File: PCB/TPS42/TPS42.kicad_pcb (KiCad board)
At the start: 2 copper layers, 138.1 x 89.7 mm, 81 parts, among them J1 PJ-320A, J11 Conn_01x06, J13 Conn_01x09, J14 FH12-10S-0.5SH, J2 Conn_01x09, J3 TP Sensor Module, J4 TP Module, J6 OLED, J7 TrackPoint, J8 Battery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

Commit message: Further footprint changes
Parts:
- C1: footprint TPS42:C_THT_SMD_0805_HandSolder_Reversable -> TPS42:C_0603_1608Metric_Pad1.08x0.95mm_HandSolder_Reversable
- C2, C3, C4: footprint Capacitor_SMD:C_0603_1608Metric_Pad1.08x0.95mm_HandSolder -> TPS42:C_0603_1608Metric_Pad1.08x0.95mm_HandSolder_Reversable
- R1, R2, R3, R4, R5: footprint TPS42:Resistor-TH_SMD -> TPS42:R_0603_1608Metric_Pad0.98x0.95mm_HandSolder_Reversable
- R6: footprint Resistor_SMD:R_0603_1608Metric_Pad0.98x0.95mm_HandSolder -> TPS42:R_0603_1608Metric_Pad0.98x0.95mm_HandSolder_Reversable
- moved C1 6.59 mm to (139.9, 172.4)

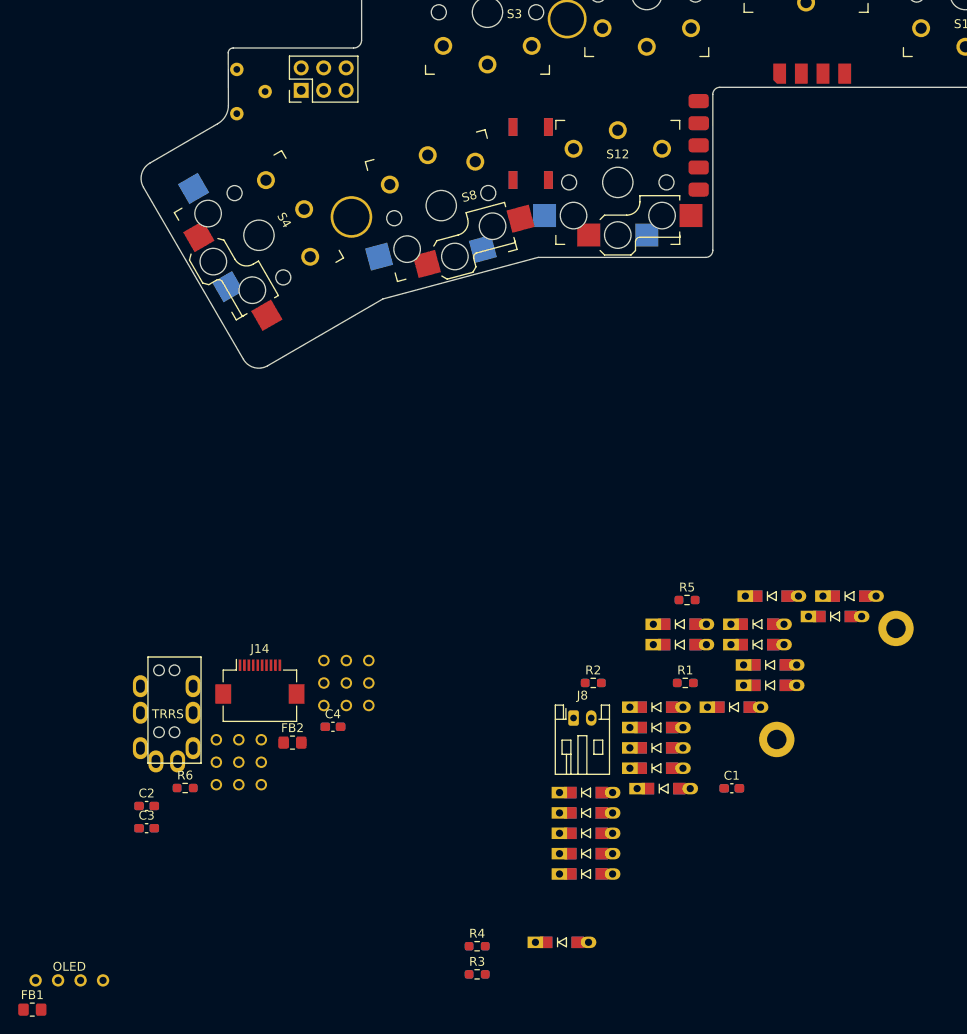
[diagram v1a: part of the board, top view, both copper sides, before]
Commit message: replaced diode footprint
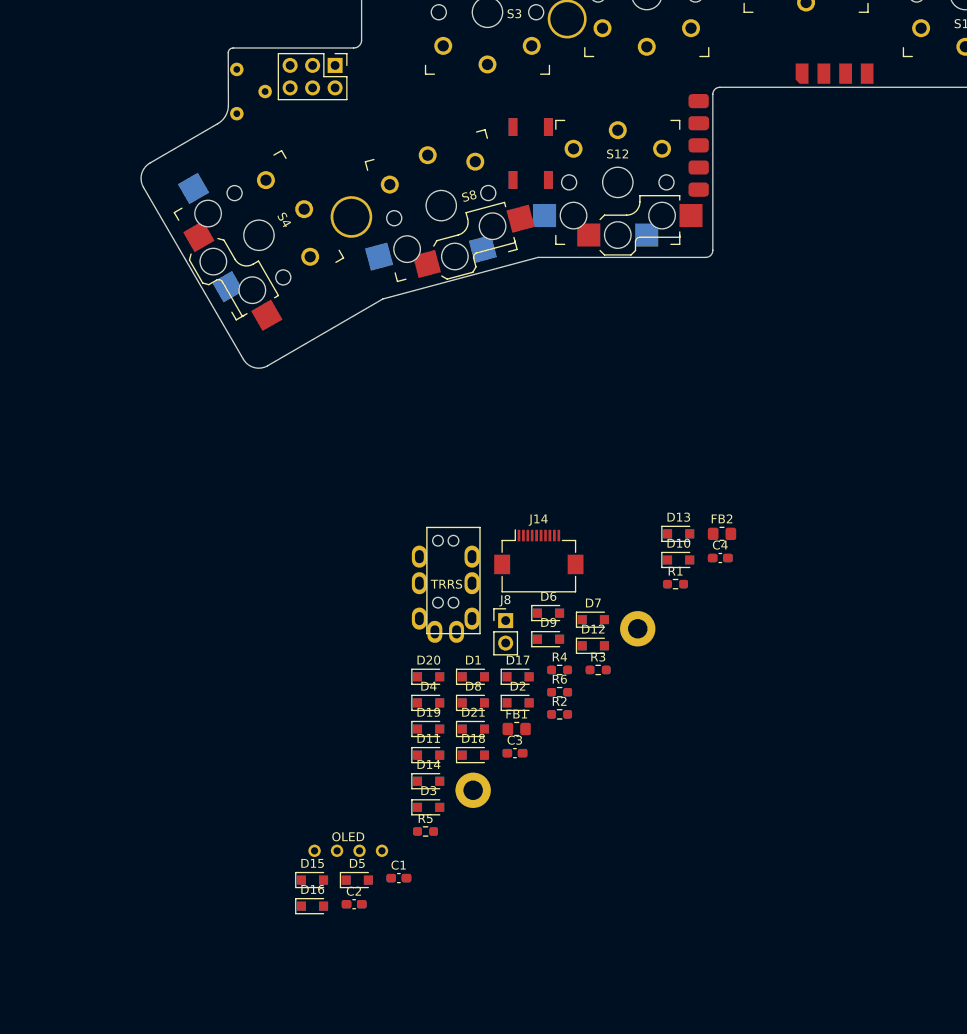
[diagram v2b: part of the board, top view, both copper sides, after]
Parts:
- removed J13, J2: Conn_01x09, TPS42:Connector_Reversable_3x3
- D1, D10, D11, D12, D13, D14, D15, D16, D17, D18, D19, D2, D20, D21, D3, D4, D5, D6, D7, D8, D9: footprint TPS42:D3_TH_SMD_v2 -> TPS42:D_SOD-323_HandSoldering_Reversable
- J8: footprint Connector_JST:JST_PH_S2B-PH-K_1x02_P2.00mm_Horizontal -> Connector_PinHeader_2.54mm:PinHeader_1x02_P2.54mm_Vertical
- moved FB1 63.3 mm to (115.6, 165.7)
- moved D16 59.5 mm to (92.5, 185.8)
- moved FB2 54.0 mm to (138.8, 143.7)
- moved D5 52.5 mm to (97.6, 182.8)
- moved C4 47.7 mm to (138.6, 146.4)
- moved D18 43.8 mm to (110.7, 168.7)
- moved R6 43.7 mm to (120.4, 161.6)
- moved C3 42.5 mm to (115.4, 168.5)
- moved D15 41.6 mm to (92.5, 182.8)
- moved D19 41.6 mm to (105.6, 165.7)
- moved R5 39.5 mm to (105.3, 177.3)
- moved D2 39.3 mm to (115.7, 162.8)
- moved C1 39.0 mm to (102.3, 182.6)
- moved R3 37.0 mm to (124.8, 159.1)
- moved U2 34.8 mm to (110.7, 172.7)
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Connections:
- J11 pad 4: VCC -> SERIAL
- J11 pad 5: SERIAL -> VCC

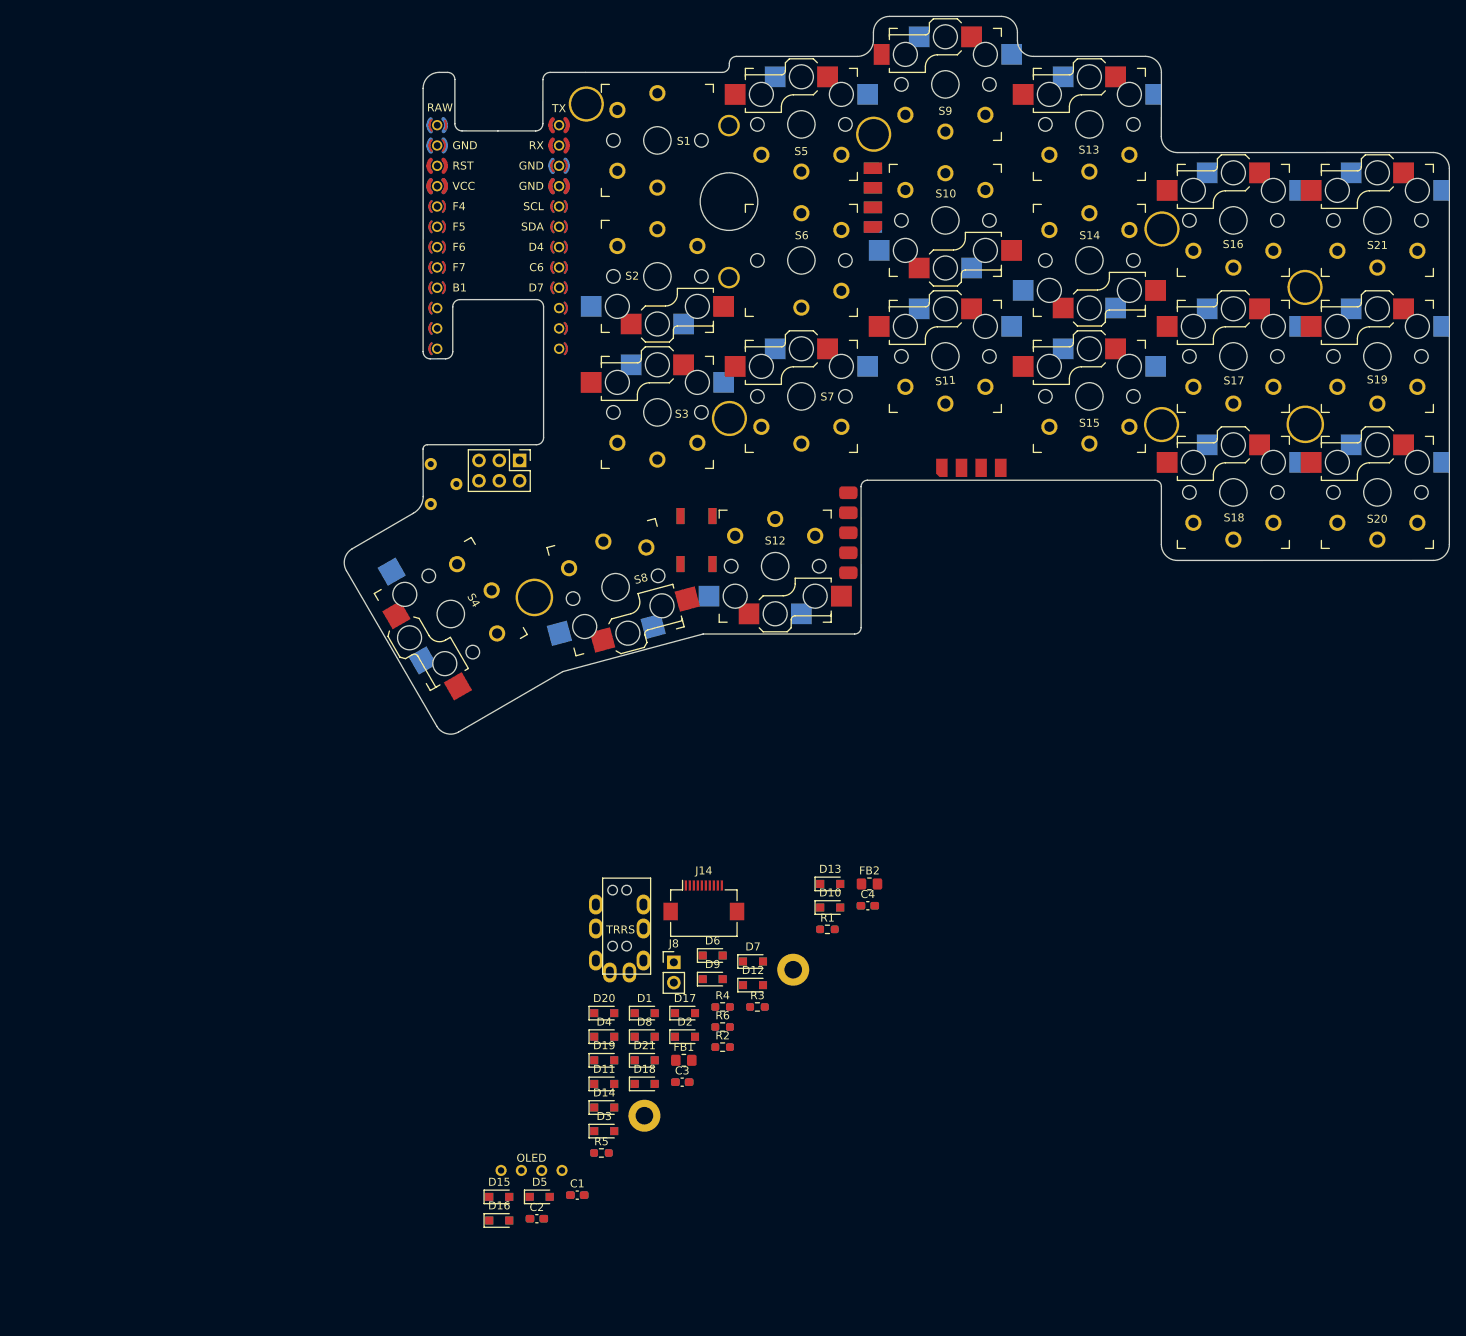
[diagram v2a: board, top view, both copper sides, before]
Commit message: breakoff column added
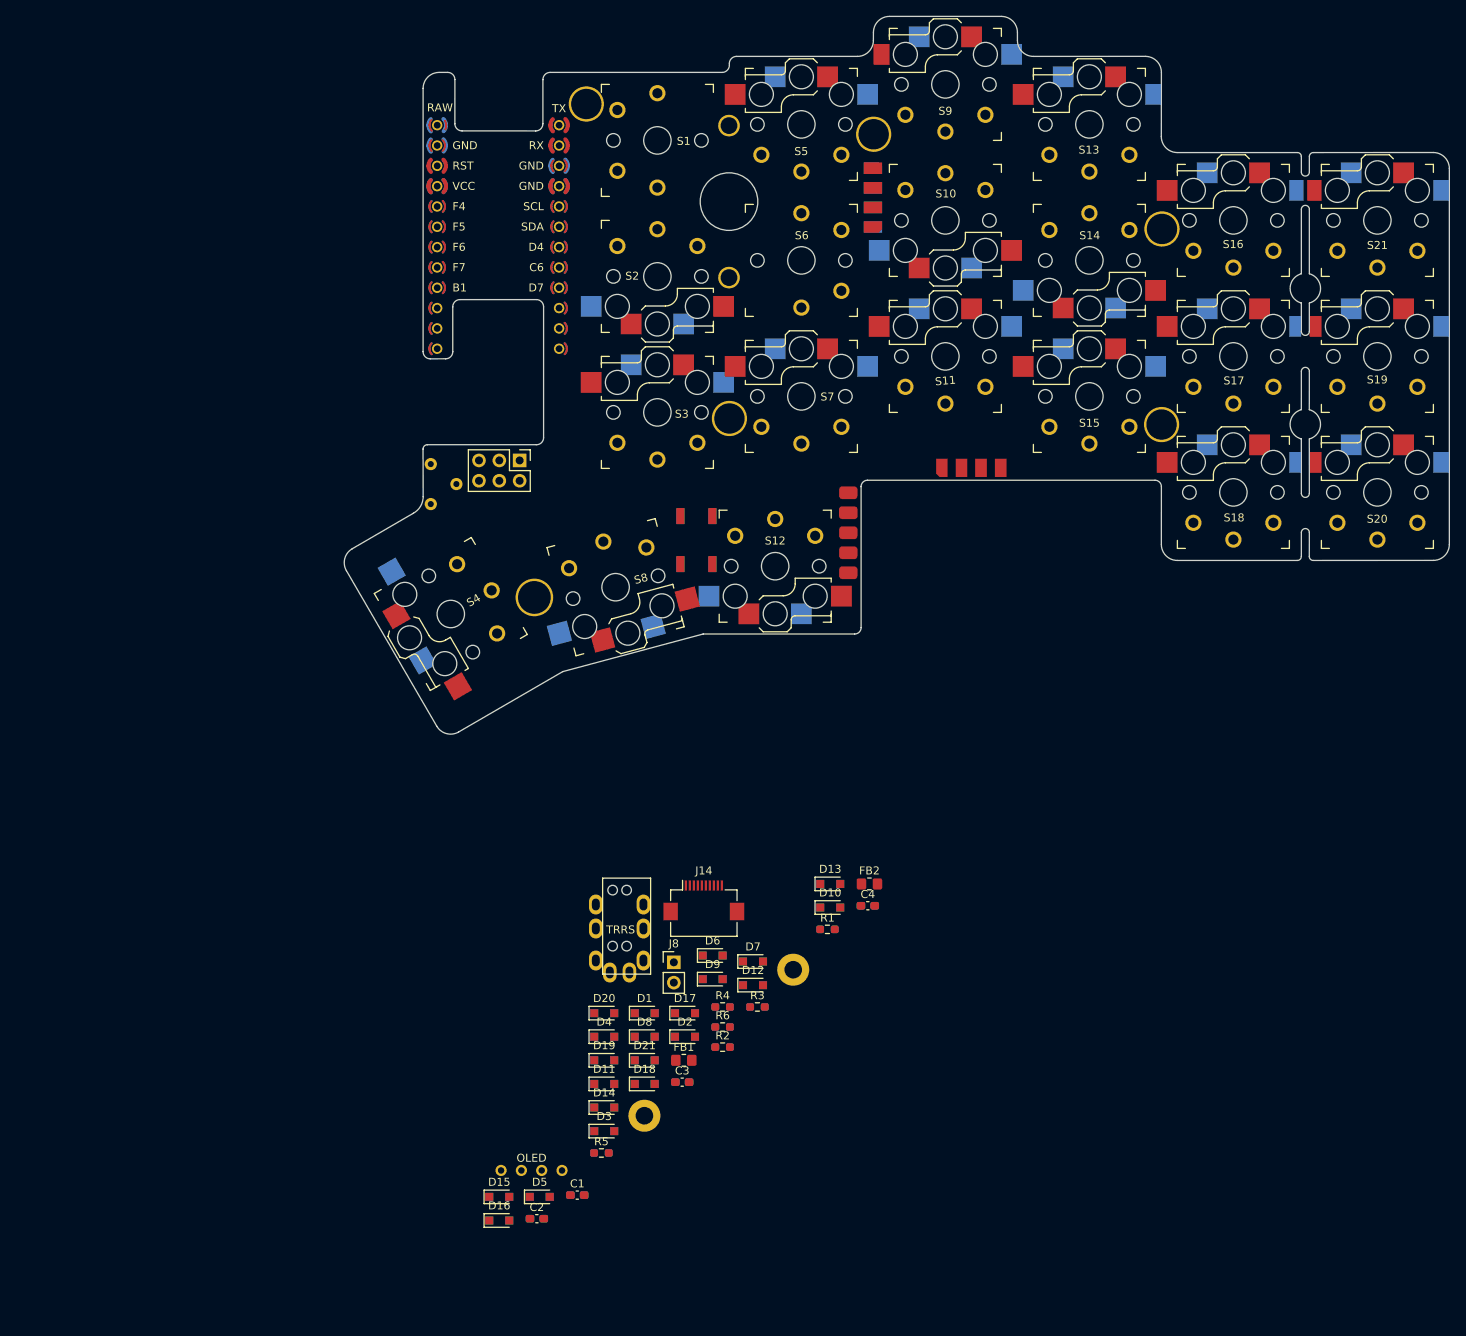
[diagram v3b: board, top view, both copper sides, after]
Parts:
- removed U10, U6: Hole, TPS42:HOLE_M2_TH
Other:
- outline, holes or cut-outs redrawn
